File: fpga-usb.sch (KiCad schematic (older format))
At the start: 8 parts, among them J1 ZX62-B-5PA11, P1 CONN_6X2, U1 MAX3453EEUD

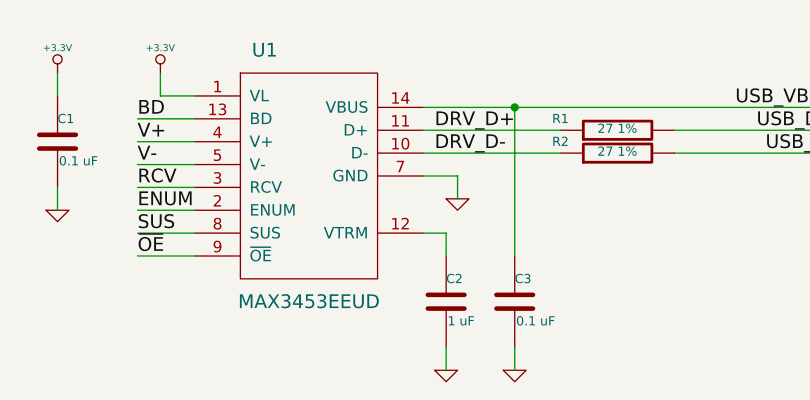
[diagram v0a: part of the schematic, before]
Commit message: Use MAX3453EETE instead of a discontinued part
This commit updates schematic only.
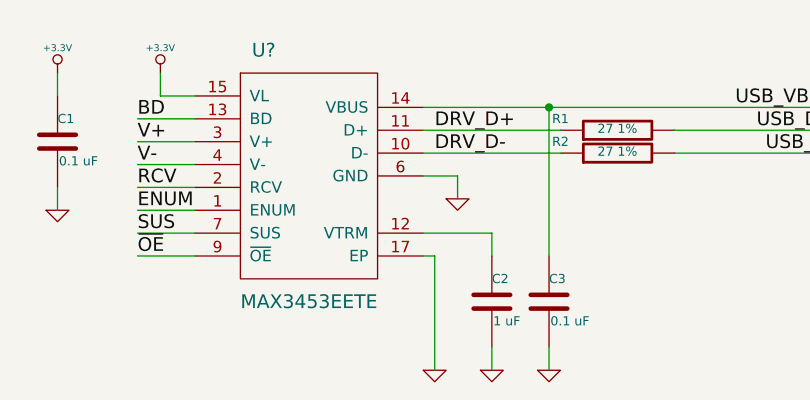
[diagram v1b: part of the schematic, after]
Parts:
- removed U1: MAX3453EEUD, Housings_SSOP:TSSOP-14_4.4x5mm_Pitch0.65mm, symbol MAX3453EEUD
- added U?: MAX3453EETE, symbol MAX3453EETE
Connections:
- net +3.3V: now also U?.15 (VL)
- net BD: now also U?.13 (BD)
- net DRV_D+: now also U?.11 (D+)
- net DRV_D-: now also U?.10 (D-)
- net ENUM: now also U?.1 (ENUM)
- net GND: now also U?.17 (EP), U?.6 (GND)
- net RCV: now also U?.2 (RCV)
- net SUS: now also U?.7 (SUS)
- net USB_VBUS: now also U?.14 (VBUS)
- net V+: now also U?.3 (V+)
- net V-: now also U?.4 (V-)
- net ~OE: now also U?.9 (~OE)
- net at C2.1: now also U?.12 (VTRM)
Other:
- moved on the sheet: C2, C3
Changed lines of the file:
@@
 Comment4 ""
 $EndDescr
-$Comp
-L MAX3453EEUD U1
-U 1 1 5607537E
-P 5350 3300
-F 0 "U1" H 5100 3850 60  0000 L CNN
-F 1 "MAX3453EEUD" H 5350 2750 60  0000 C CNN
-F 2 "Housings_SSOP:TSSOP-14_4.4x5mm_Pitch0.65mm" H 5350 3350 60  0001 C CNN
-F 3 "" H 5350 3350 60  0000 C CNN
-	1    5350 3300
-	1    0    0    -1
-$EndComp
 Wire Wire Line
 	5850 3000 7650 3000
@@
 L C C2
 U 1 1 5607541C
-P 5950 3850
-F 0 "C2" H 5950 3950 40  0000 L CNN
-F 1 "1 uF" H 5956 3765 40  0000 L CNN
-F 2 "gps:C0402" H 5988 3700 30  0001 C CNN
-F 3 "" H 5950 3850 60  0000 C CNN
-	1    5950 3850
-	1    0    0    -1
-$EndComp
-Wire Wire Line
-	5850 3550 5950 3550
-Wire Wire Line
-	5950 3550 5950 3650
+P 6150 3850
+F 0 "C2" H 6150 3950 40  0000 L CNN
+F 1 "1 uF" H 6156 3765 40  0000 L CNN
+F 2 "gps:C0402" H 6188 3700 30  0001 C CNN
+F 3 "" H 6150 3850 60  0000 C CNN
+	1    6150 3850
+	1    0    0    -1
+$EndComp
+Wire Wire Line
+	5850 3550 6150 3550
+Wire Wire Line
+	6150 3550 6150 3650
 $Comp
 L GND #PWR02
 U 1 1 56075449
-P 5950 4150
-F 0 "#PWR02" H 5950 4150 30  0001 C CNN
-F 1 "GND" H 5950 4080 30  0001 C CNN
-F 2 "" H 5950 4150 60  0000 C CNN
-F 3 "" H 5950 4150 60  0000 C CNN
-	1    5950 4150
-	1    0    0    -1
-$EndComp
-Wire Wire Line
-	5950 4050 5950 4150
+P 6150 4150
+F 0 "#PWR02" H 6150 4150 30  0001 C CNN
+F 1 "GND" H 6150 4080 30  0001 C CNN
+F 2 "" H 6150 4150 60  0000 C CNN
+F 3 "" H 6150 4150 60  0000 C CNN
+	1    6150 4150
+	1    0    0    -1
+$EndComp
+Wire Wire Line
+	6150 4050 6150 4150
 $Comp
 L C C3
 U 1 1 5607547A
-P 6250 3850
-F 0 "C3" H 6250 3950 40  0000 L CNN
-F 1 "0.1 uF" H 6256 3765 40  0000 L CNN
-F 2 "gps:C0402" H 6288 3700 30  0001 C CNN
-F 3 "" H 6250 3850 60  0000 C CNN
-	1    6250 3850
+P 6400 3850
+F 0 "C3" H 6400 3950 40  0000 L CNN
+F 1 "0.1 uF" H 6406 3765 40  0000 L CNN
+F 2 "gps:C0402" H 6438 3700 30  0001 C CNN
+F 3 "" H 6400 3850 60  0000 C CNN
+	1    6400 3850
 	1    0    0    -1
 $EndComp
@@
 L GND #PWR03
 U 1 1 560754D2
-P 6250 4150
-F 0 "#PWR03" H 6250 4150 30  0001 C CNN
-F 1 "GND" H 6250 4080 30  0001 C CNN
-F 2 "" H 6250 4150 60  0000 C CNN
-F 3 "" H 6250 4150 60  0000 C CNN
-	1    6250 4150
-	1    0    0    -1
-$EndComp
-Wire Wire Line
-	6250 4150 6250 4050
-Wire Wire Line
-	6250 3650 6250 3000
-Connection ~ 6250 3000
+P 6400 4150
+F 0 "#PWR03" H 6400 4150 30  0001 C CNN
+F 1 "GND" H 6400 4080 30  0001 C CNN
+F 2 "" H 6400 4150 60  0000 C CNN
+F 3 "" H 6400 4150 60  0000 C CNN
+	1    6400 4150
+	1    0    0    -1
+$EndComp
+Wire Wire Line
+	6400 4150 6400 4050
+Wire Wire Line
+	6400 3650 6400 3000
+Connection ~ 6400 3000
 $Comp
 L R R2
@@
 Text Label 5900 3200 0    60   ~ 0
 DRV_D-
+$Comp
+L MAX3453EETE U?
+U 1 1 563673BF
+P 5350 3300
+F 0 "U?" H 5100 3850 60  0000 L CNN
+F 1 "MAX3453EETE" H 5350 2750 60  0000 C CNN
+F 2 "" H 5350 3350 60  0000 C CNN
+F 3 "" H 5350 3350 60  0000 C CNN
+	1    5350 3300
+	1    0    0    -1
+$EndComp
+$Comp
+L GND #PWR?
+U 1 1 563674DF
+P 5900 4150
+F 0 "#PWR?" H 5900 4150 30  0001 C CNN
+F 1 "GND" H 5900 4080 30  0001 C CNN
+F 2 "" H 5900 4150 60  0000 C CNN
+F 3 "" H 5900 4150 60  0000 C CNN
+	1    5900 4150
+	1    0    0    -1
+$EndComp
+Wire Wire Line
+	5900 4150 5900 3650
+Wire Wire Line
+	5900 3650 5850 3650
 $EndSCHEMATC
